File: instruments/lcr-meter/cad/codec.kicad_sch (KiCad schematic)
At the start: 37 parts, among them U14 TAC5112, U15 3.3V AP2112K

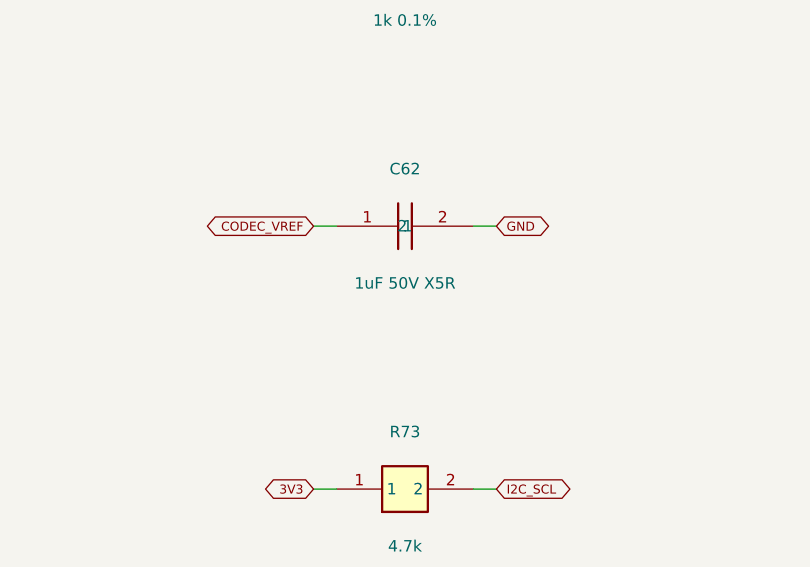
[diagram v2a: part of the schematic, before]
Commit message: lcr-meter Rev F: datasheet audit fixes (TPS65131 start-up sequencer, 5 V bulk, VREF, coil feed, test pads)
Seven independent datasheet reviews (validation/datasheet-audit-rev-f/, dispositions in its README).
One real board failure: with ENP = ENN = 3V3 both TPS65131 converters start together against
the TPS2553's 0.99 A minimum limit, and a full power-up model shows the boost can start at 5 V
= 2.1 V while U16 is still charging the node, so the board hiccups.

- U17 LM3880MF-1AA sequences ENP, then ENN 10 ms later, through open-drain flags with
  R119/R120 pull-ups to 3V3, so the EN pins never exceed VIN + 0.3 V. RC delays on the pins
  were modelled and rejected.
- C117 330 uF polymer on 5 V. R110 stays 24k: a 1.8 A limit fails the IPC-2152 rule.
- startup_surge.py: power-up from attach, 128 corners all pass, 5 V >= 3.86 V; the board
  before the audit fails 0 / 128.
- C113 4.7 uF (hot-plug), R101 1 ohm (RESET coil margin), C62 2.2 uF (TAC5112 VREF minimum
  1 uF): value-only changes.
- TP15-TP21: I2S x4 + GND, USB_VBUS + GND.
- package_cad.py now requires a placement audit for polarized caps.

Analog copper is identical to 6ae693082 (copper_delta.sh), so the extraction and stability
results carry over. ERC 0, DRC 0/0/0, JLC fab pass PASS, independent check 0 findings,
IPC-2152 0 FAIL, regulators 51 PASS / 2 FLAG. Board SHA256 780bf3ae...

Co-Authored-By: Claude Opus 5.5 <noreply@anthropic.com>
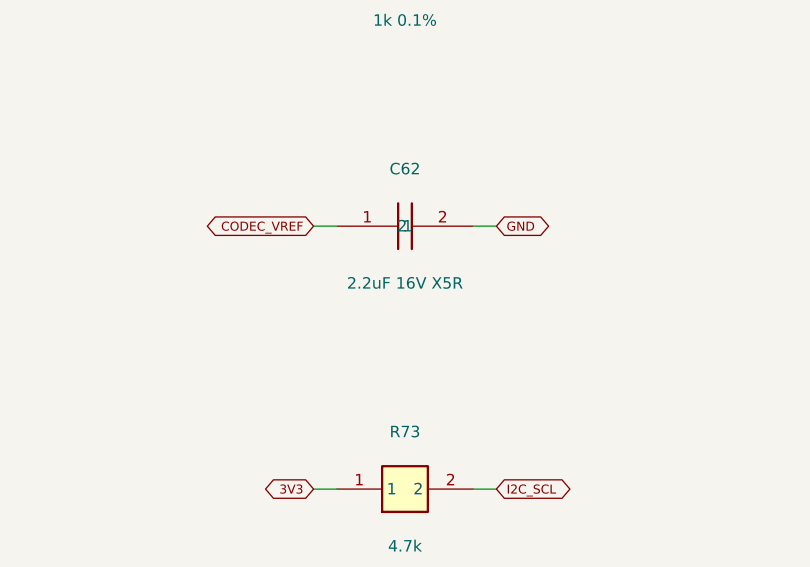
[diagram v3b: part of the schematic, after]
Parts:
- C62: value 1uF 50V X5R -> 2.2uF 16V X5R; LCSC C15849 -> C23630; MPN CL10A105KB8NNNC -> CL10A225KO8NNNC; Unit_USD 0.0153 -> 0.0119
